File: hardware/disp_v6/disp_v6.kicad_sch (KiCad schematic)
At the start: 241 parts, among them J1 RJ45, J12 Conn_01x06, J2 Conn_01x06_Pin, J3 Conn_01x05_Pin, J4 Conn_01x04_Pin, J5 Conn_01x06_Pin, J6 Conn_01x04_Pin, J7 Conn_01x04_Pin, J8 Conn_01x02, J9 Conn_02x10_Odd_Even, Q1 2N7002, Q10 2N7002, Q2 2N7002, Q3 2N7002, Q4 2N7002, Q5 2N7002, Q6 2N7002, Q7 2N7002, Q8 2N7002, Q9 2N7002, U1 ADA4807-1, U10 STM32F405RGTx, U11 AMS1117-3.3, U12 BA50DD0WHFP-TR, U13 M24C02-RMN, U2 SN74LVC1G14DBV, U3 SN74LVC1G14DBV, U4 ADA4807-1, U5 ADA4807-1, U6 TLV3603DCKR, U7 SN74LVC1G14DBV, U8 TLV3603DCKR, U9 L78L05_SOT89, X2 GTXO-14V (2.048MHz), Y1 AOCJY4A-10.000MHZ-SW, Y2 16MHz

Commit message: start clean up of disp 6
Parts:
- removed ANT1, ANT2, ANT3, ANT4, ANT5, ANT6: U.FL-R-SMT-1, blinky_footprints:U.FL-R-SMT-1, symbol blinky:U.FL-R-SMT-1
- removed C1, C10, C11, C17, C18, C2, C25, C26, C30, C33, C45, C46, C47, C48, C49, C9: 100nF, Capacitor_SMD:C_0402_1005Metric, symbol Device:C_Small
- removed C12, C14, C19, C23, C5, C7: 150pF, Capacitor_SMD:C_0603_1608Metric, symbol Device:C_Small
- removed C13, C20, C8: 330pF, Capacitor_SMD:C_0603_1608Metric, symbol Device:C_Small
- removed C15, C22, C6: 220pF, Capacitor_SMD:C_0603_1608Metric, symbol Device:C_Small
- removed C16, C21, C3: 1nF, Capacitor_SMD:C_0603_1608Metric, symbol Device:C_Small
- removed C24, C27, C37: 100nF, Capacitor_SMD:C_0603_1608Metric, symbol Device:C_Small
- removed C28, C29: 33pF, Capacitor_SMD:C_0603_1608Metric, symbol Device:C
- removed C34, C43: 10uF, Capacitor_Tantalum_SMD:CP_EIA-3216-18_Kemet-A, symbol Device:C_Polarized
- removed C35, C40: 2.2uF, Capacitor_SMD:C_0603_1608Metric, symbol Device:C_Small
- removed C4: 47pF, Capacitor_SMD:C_0805_2012Metric, symbol Device:C_Small
- removed C42, C44: 33uF, Capacitor_Tantalum_SMD:CP_EIA-3528-21_Kemet-B, symbol Device:C_Polarized
- removed FB1: 120Ω@100MHz, Resistor_SMD:R_0603_1608Metric, symbol Device:FerriteBead_Small
- removed H3: M2, MountingHole:MountingHole_2.2mm_M2, symbol Mechanical:MountingHole
- removed J1: RJ45, Connector_RJ:RJ45_Amphenol_RJHSE5380, symbol Connector:RJ45
- removed J12: Conn_01x06, Connector_JST:JST_PH_S6B-PH-SM4-TB_1x06-1MP_P2.00mm_Horizontal, symbol Connector_Generic:Conn_01x06
- removed J2, J5: Conn_01x06_Pin, Connector_PinHeader_2.54mm:PinHeader_1x06_P2.54mm_Vertical, symbol Connector:Conn_01x06_Pin
- removed J3: Conn_01x05_Pin, Connector_PinHeader_2.54mm:PinHeader_1x05_P2.54mm_Vertical, symbol Connector:Conn_01x05_Pin
- removed J4, J6, J7: Conn_01x04_Pin, Connector_PinHeader_2.54mm:PinHeader_1x04_P2.54mm_Vertical, symbol Connector:Conn_01x04_Pin
- removed J8: Conn_01x02, Connector_JST:JST_PH_S2B-PH-SM4-TB_1x02-1MP_P2.00mm_Horizontal, symbol Connector_Generic:Conn_01x02
- removed JP1: SolderJumper_2_Bridged, Jumper:SolderJumper-2_P1.3mm_Bridged_RoundedPad1.0x1.5mm, symbol Jumper:SolderJumper_2_Bridged
- removed L1, L2, L3, L4, L5, L6: 1uF, Inductor_SMD:L_0805_2012Metric, symbol Device:L_Small
- removed R1, R15, R16: 100R, Resistor_SMD:R_0603_1608Metric, symbol Device:R_Small_US
- removed R10, R2, R6: 510R, Resistor_SMD:R_0603_1608Metric, symbol Device:R_Small_US
- removed R11, R3, R7: 49R9, Resistor_SMD:R_0603_1608Metric, symbol Device:R_Small_US
- removed R12, R13: 1K5, Resistor_SMD:R_0805_2012Metric, symbol Device:R_Small_US
- removed R14: 330R, Resistor_SMD:R_0805_2012Metric, symbol Device:R_Small_US
- removed R17: 20R, Resistor_SMD:R_0805_2012Metric, symbol Device:R_Small_US
- removed R18, R21: 130K, Resistor_SMD:R_0603_1608Metric, symbol Device:R_Small_US
- removed R19, R20, R22, R24, R5, R54, R60, R61, R62, R63, R64: 1K0, Resistor_SMD:R_0603_1608Metric, symbol Device:R_Small_US
- removed R23: 22K, Resistor_SMD:R_0805_2012Metric, symbol Device:R_Small_US
- removed R25: 270R, Resistor_SMD:R_0603_1608Metric, symbol Device:R_Small_US
- removed R26: 22R0, Resistor_SMD:R_0603_1608Metric, symbol Device:R_Small_US
- removed R27, R28, R32: 4K7, Resistor_SMD:R_0603_1608Metric, symbol Device:R_US
- removed R4: 200R, Resistor_SMD:R_0805_2012Metric, symbol Device:R_Small_US
- removed R58, R59: 1K5, Resistor_SMD:R_0603_1608Metric, symbol Device:R_Small_US
- removed R8: 270R, Resistor_SMD:R_0805_2012Metric, symbol Device:R_Small_US
- removed R9: 2R, Resistor_SMD:R_0805_2012Metric, symbol Device:R_Small_US
- removed RV1: 20K, Potentiometer_SMD:Potentiometer_Bourns_3314G_Vertical, symbol Device:R_Potentiometer_US
- removed S1, S2: 147873-2, SW_147873-2, symbol blinky:147873-2
- removed TP1, TP10, TP11, TP12, TP13, TP14, TP15, TP16, TP18, TP19, TP2, TP3, TP4, TP5, TP6, TP7, TP8, TP9: ~, TestPoint:TestPoint_THTPad_D1.5mm_Drill0.7mm, symbol Connector:TestPoint
- removed U1, U4, U5: ADA4807-1, Package_TO_SOT_SMD:SOT-23-6, symbol Amplifier_Operational:ADA4807-1
- removed U10: STM32F405RGTx, Package_QFP:LQFP-64_10x10mm_P0.5mm, symbol MCU_ST_STM32F4:STM32F405RGTx
- removed U12: BA50DD0WHFP-TR, blinky_footprints:DPAK172P1054X200-6N, symbol blinky:BA50DD0WHFP-TR
- removed U13: M24C02-RMN, Package_SO:SOIC-8_3.9x4.9mm_P1.27mm, symbol Memory_EEPROM:M24C02-RMN
- removed U2, U3, U7: SN74LVC1G14DBV, Package_TO_SOT_SMD:SOT-23-5, symbol 74xGxx:SN74LVC1G14DBV
- removed U6: TLV3603DCKR, blinky_footprints:SC70_DCK_TEX, symbol blinky:TLV3603DCKR
- removed U8: TLV3603DCKR, SC70_DCK_TEX, symbol blinky:TLV3603DCKR
- removed U9: L78L05_SOT89, Package_TO_SOT_SMD:SOT-89-3, symbol Regulator_Linear:L78L05_SOT89
- removed X2: GTXO-14V (2.048MHz), Oscillator:Oscillator_DIP-14, symbol Oscillator:GTXO-14V
- removed Y1: AOCJY4A-10.000MHZ-SW, blinky_footprints:XTAL_AOCJY4A-10.000MHZ-SW, symbol blinky:AOCJY4A-10.000MHZ-SW
- removed Y2: 16MHz, Crystal:Crystal_SMD_3225-4Pin_3.2x2.5mm, symbol Device:Crystal_GND24
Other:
- note removed: "12 MHz 5th Order Butterworth Lowpass"
- note removed: "3.1 MHz RC Highpass filter"
- note removed: "I2C Addr: 0x50 (7bit)"

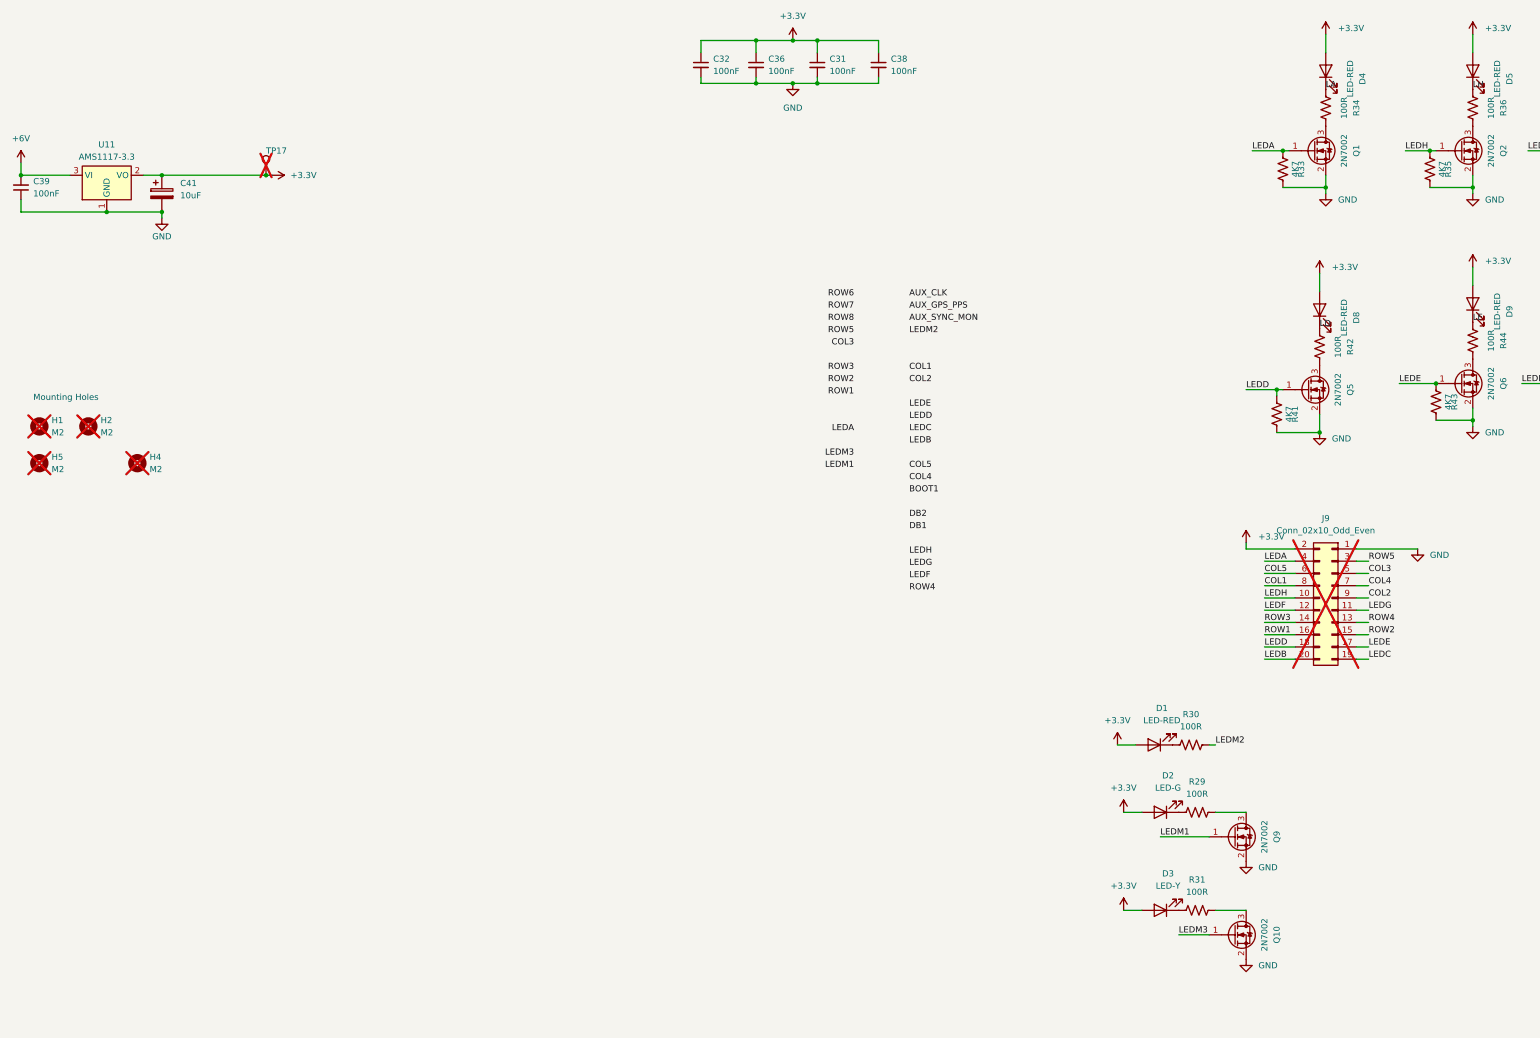
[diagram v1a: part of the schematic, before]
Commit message: first route of disp board
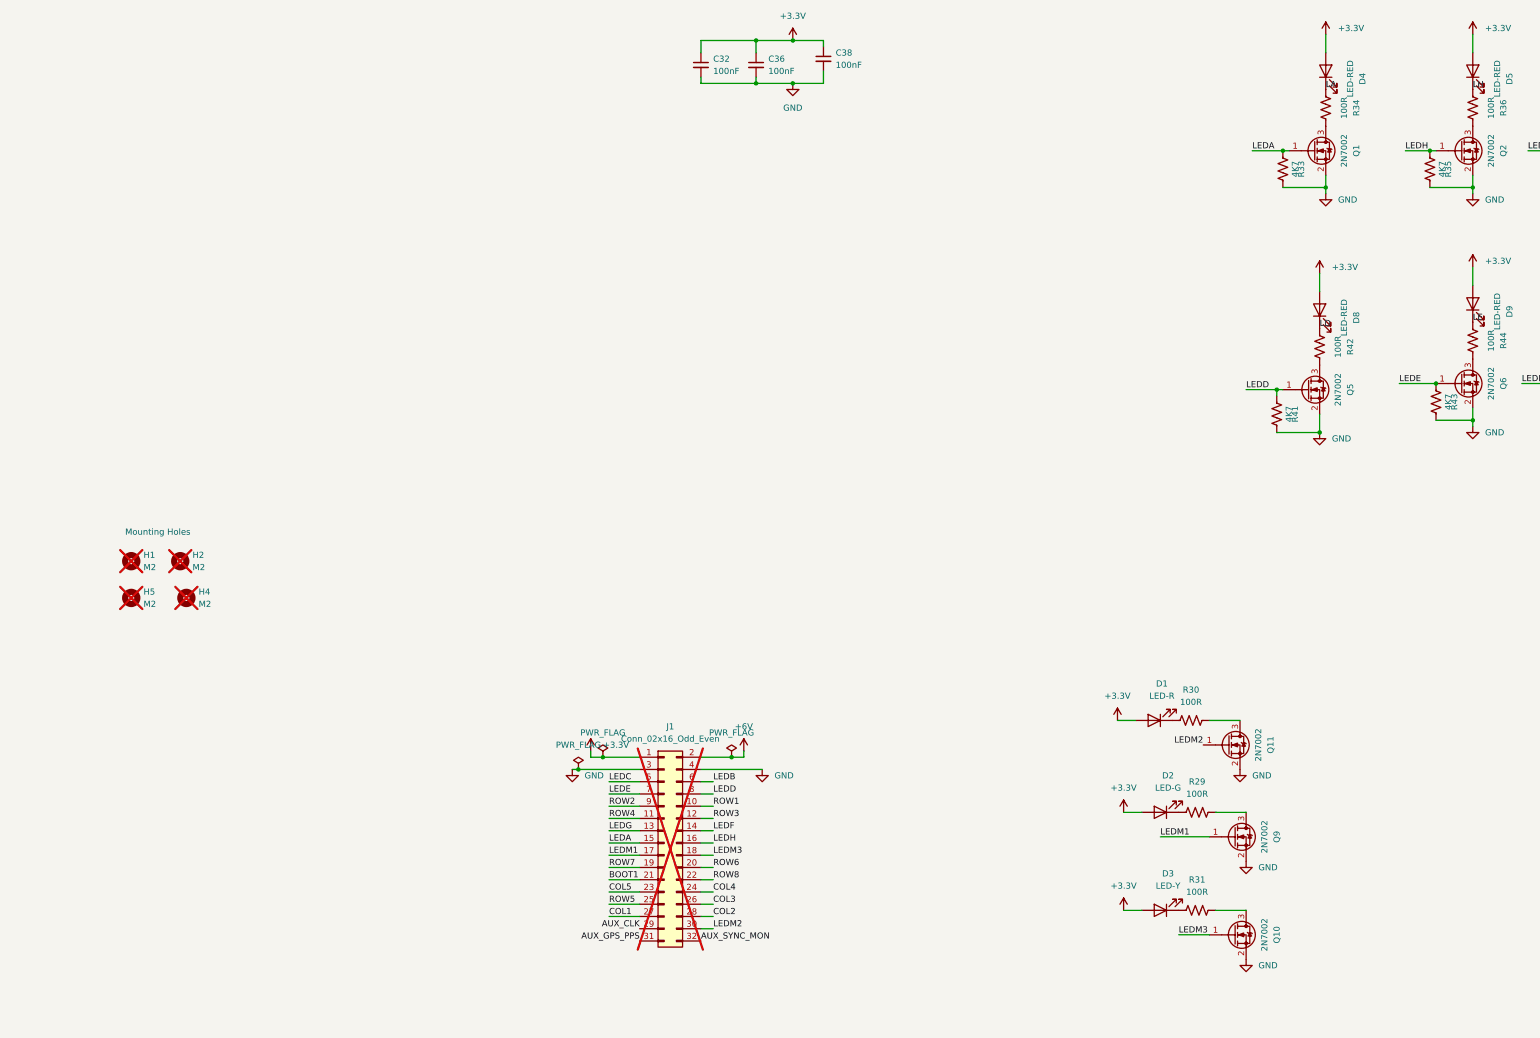
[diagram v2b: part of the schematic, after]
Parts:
- removed C31, C39: 100nF, Capacitor_SMD:C_0402_1005Metric, symbol Device:C_Small
- removed C41: 10uF, Capacitor_Tantalum_SMD:CP_EIA-3216-18_Kemet-A, symbol Device:C_Polarized
- removed J9: Conn_02x10_Odd_Even, Connector_PinHeader_2.54mm:PinHeader_2x10_P2.54mm_Vertical, symbol Connector_Generic:Conn_02x10_Odd_Even
- removed TP17: ~, TestPoint:TestPoint_THTPad_D1.5mm_Drill0.7mm, symbol Connector:TestPoint
- removed U11: AMS1117-3.3, Package_TO_SOT_SMD:SOT-223-3_TabPin2, symbol Regulator_Linear:AMS1117-3.3
- added J1: Conn_02x16_Odd_Even, Connector_PinHeader_2.54mm:PinHeader_2x16_P2.54mm_Vertical, symbol Connector_Generic:Conn_02x16_Odd_Even
- added Q11: 2N7002, Package_TO_SOT_SMD:SOT-23, symbol Transistor_FET:2N7002
- D1: value LED-RED -> LED-R
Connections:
- net +3.3V: now also J1.1 (Pin_1)
- net +6V: now also J1.2 (Pin_2)
- net AUX_CLK: now also J1.29 (Pin_29)
- net AUX_GPS_PPS: now also J1.31 (Pin_31)
- net AUX_SYNC_MON: now also J1.32 (Pin_32)
- net BOOT1: now also J1.21 (Pin_21)
- net COL1: now also J1.27 (Pin_27)
- net COL2: now also J1.28 (Pin_28)
- net COL3: now also J1.26 (Pin_26)
- net COL4: now also J1.24 (Pin_24)
- net COL5: now also J1.23 (Pin_23)
- net GND: now also J1.3 (Pin_3), J1.4 (Pin_4), Q11.2 (S)
- net LEDA: now also J1.15 (Pin_15)
- net LEDB: now also J1.6 (Pin_6)
- net LEDC: now also J1.5 (Pin_5)
- net LEDD: now also J1.8 (Pin_8)
- net LEDE: now also J1.7 (Pin_7)
- net LEDF: now also J1.14 (Pin_14)
- net LEDG: now also J1.13 (Pin_13)
- net LEDH: now also J1.16 (Pin_16)
- net LEDM1: now also J1.17 (Pin_17)
- net LEDM2: now also J1.30 (Pin_30), Q11.1 (G); no longer R30.2
- net LEDM3: now also J1.18 (Pin_18)
- net ROW1: now also J1.10 (Pin_10)
- net ROW2: now also J1.9 (Pin_9)
- net ROW3: now also J1.12 (Pin_12)
- net ROW4: now also J1.11 (Pin_11)
- net ROW5: now also J1.25 (Pin_25)
- net ROW6: now also J1.20 (Pin_20)
- net ROW7: now also J1.19 (Pin_19)
- net ROW8: now also J1.22 (Pin_22)
- new net: Q11.3 (D), R30.2
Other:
- moved on the sheet: C38, D1, H1, H2, H4, H5, R30

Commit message: reduce schematic paper size
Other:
- title: Blinky V4 -> Disp V6
- moved on the sheet: C32, C36, C38, D1, D10, D11, D12, D13, D14, D15, D16, D17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

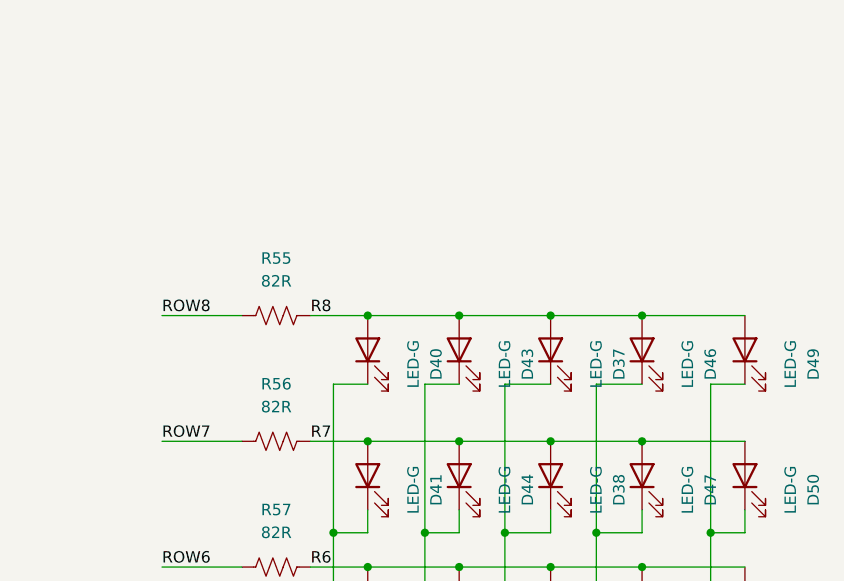
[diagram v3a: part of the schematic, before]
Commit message: add two more rows of grid lights
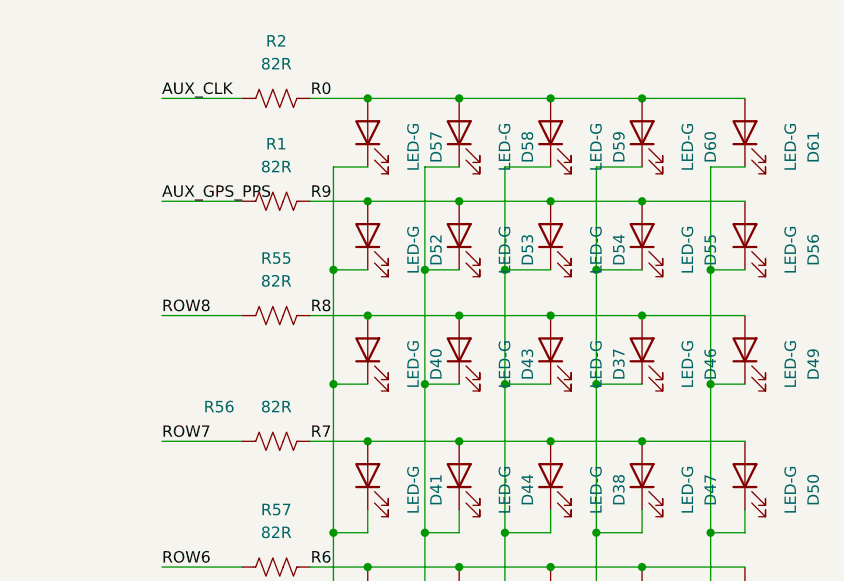
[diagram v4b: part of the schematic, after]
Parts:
- added D52, D53, D54, D55, D56, D57, D58, D59, D60, D61: LED-G, LED_SMD:LED_0603_1608Metric, symbol Device:LED
- added R1, R2: 82R, Resistor_SMD:R_0603_1608Metric, symbol Device:R_US
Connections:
- net AUX_CLK: now also R2.2
- net AUX_GPS_PPS: now also R1.2
- net COL1: now also D52.1 (K), D57.1 (K)
- net COL2: now also D53.1 (K), D58.1 (K)
- net COL3: now also D54.1 (K), D59.1 (K)
- net COL4: now also D55.1 (K), D60.1 (K)
- net COL5: now also D56.1 (K), D61.1 (K)
- new net R0: D57.2 (A), D58.2 (A), D59.2 (A), D60.2 (A), D61.2 (A), R2.1
- new net R9: D52.2 (A), D53.2 (A), D54.2 (A), D55.2 (A), D56.2 (A), R1.1

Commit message: dreive new ros off of boot0 boot1
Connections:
- net AUX_GPS_PPS: no longer R1.2
- net BOOT1: now also R1.2
- net AUX_CLK renamed BOOT0
- net AUX_SYNC_MON renamed GPS_PPS
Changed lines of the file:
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@@
     (effects (font (size 1.27 1.27)) (justify left bottom))
   )
-  (label "AUX_CLK" (at 33.02 59.69 180) (fields_autoplaced)
+  (label "BOOT0" (at 33.02 59.69 180) (fields_autoplaced)
     (effects (font (size 1.27 1.27)) (justify right bottom))
   )
-  (label "AUX_CLK" (at 171.45 25.4 0) (fields_autoplaced)
+  (label "BOOT0" (at 171.45 25.4 0) (fields_autoplaced)
     (effects (font (size 1.27 1.27)) (justify left bottom))
   )
@@
     (effects (font (size 1.27 1.27)) (justify left bottom))
   )
-  (label "AUX_GPS_PPS" (at 171.45 36.83 0) (fields_autoplaced)
+  (label "BOOT1" (at 171.45 36.83 0) (fields_autoplaced)
     (effects (font (size 1.27 1.27)) (justify left bottom))
   )
@@
     (effects (font (size 1.27 1.27)) (justify left bottom))
   )
-  (label "AUX_SYNC_MON" (at 45.72 62.23 0) (fields_autoplaced)
+  (label "GPS_PPS" (at 45.72 62.23 0) (fields_autoplaced)
     (effects (font (size 1.27 1.27)) (justify left bottom))
   )

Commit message: update rotations
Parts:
- C32, C36, C38: JLCPCB Part # (none) -> C307331; LCSC C307331 -> (none)
- D1: JLCPCB Part # (none) -> C94869; LCSC C94869 -> (none)
- D10, D11, D4, D5, D6, D7, D8, D9: value LED-RED -> LED-R; JLCPCB Part # (none) -> C94869; LCSC C94869 -> (none)
- D12, D13, D14, D15, D16, D17, D18, D19, D2, D20, D21, D22, D23, D24, D25, D26, D27, D28, D29, D30, D31, D32, D33, D34, D35, D36, D37, D38, D39, D40, D41, D42, D43, D44, D45, D46, D47, D48, D49, D50, D51, D52, D53, D54, D55, D56, D57, D58, D59, D60, D61: JLCPCB Part # (none) -> C125093; LCSC C125093 -> (none)
- D3: JLCPCB Part # (none) -> C72038; LCSC C72038 -> (none)
- Q1, Q10, Q11, Q2, Q3, Q4, Q5, Q6, Q7, Q8, Q9: JLCPCB Part # (none) -> C8545; JLCPCB Rotation Offset (none) -> 180; LCSC C8545 -> (none)
- R1, R2, R49, R50, R51, R52, R53, R55, R56, R57: JLCPCB Part # (none) -> C23255; LCSC C23255 -> (none)
- R29, R30, R31, R34, R36, R38, R40, R42, R44, R46, R48: JLCPCB Part # (none) -> C22775; LCSC C22775 -> (none)
- R33, R35, R37, R39, R41, R43, R45, R47: JLCPCB Part # (none) -> C23162; LCSC C23162 -> (none)
